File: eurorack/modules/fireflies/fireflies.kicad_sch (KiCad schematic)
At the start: 45 parts, among them J2 AudioJack2_SwitchT, J3 AudioJack2_SwitchT, J4 AudioJack2_SwitchT, J5 AudioJack2_SwitchT, SW1 SW_Push_LED, SW2 SW_Push_LED, U1 MIC5219-5.0YM5, U2 Chordata, U3 MCP4822, U4 TLC5971PWP

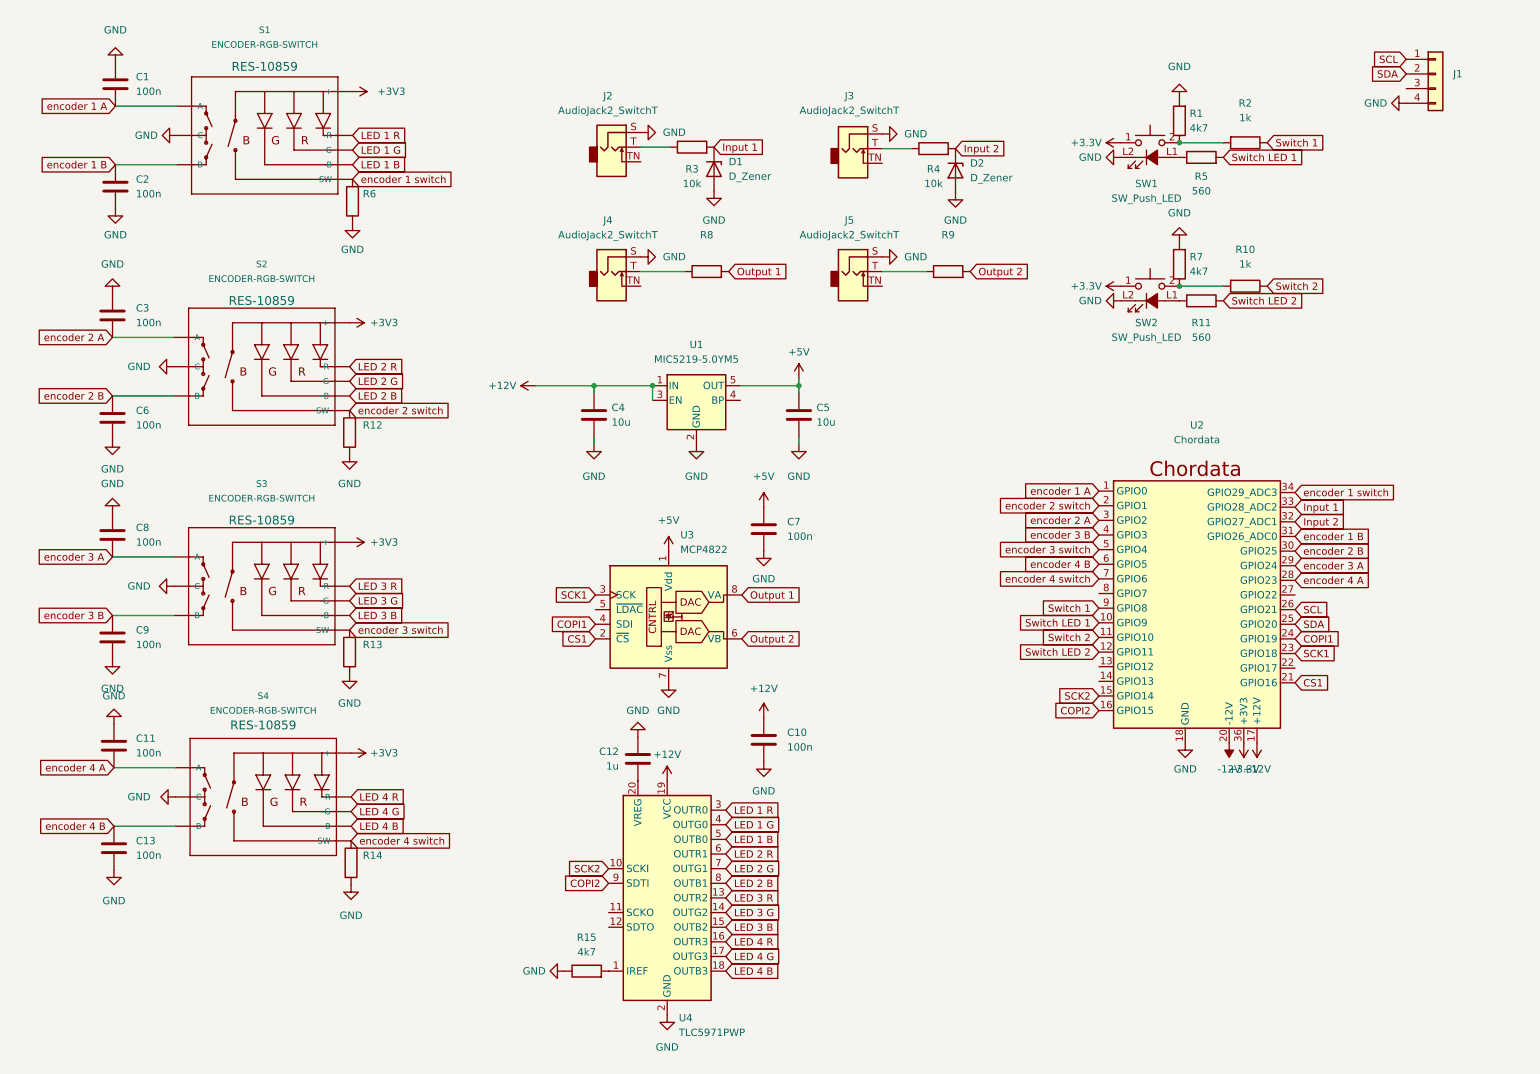
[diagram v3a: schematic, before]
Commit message: wip fireflies redesign
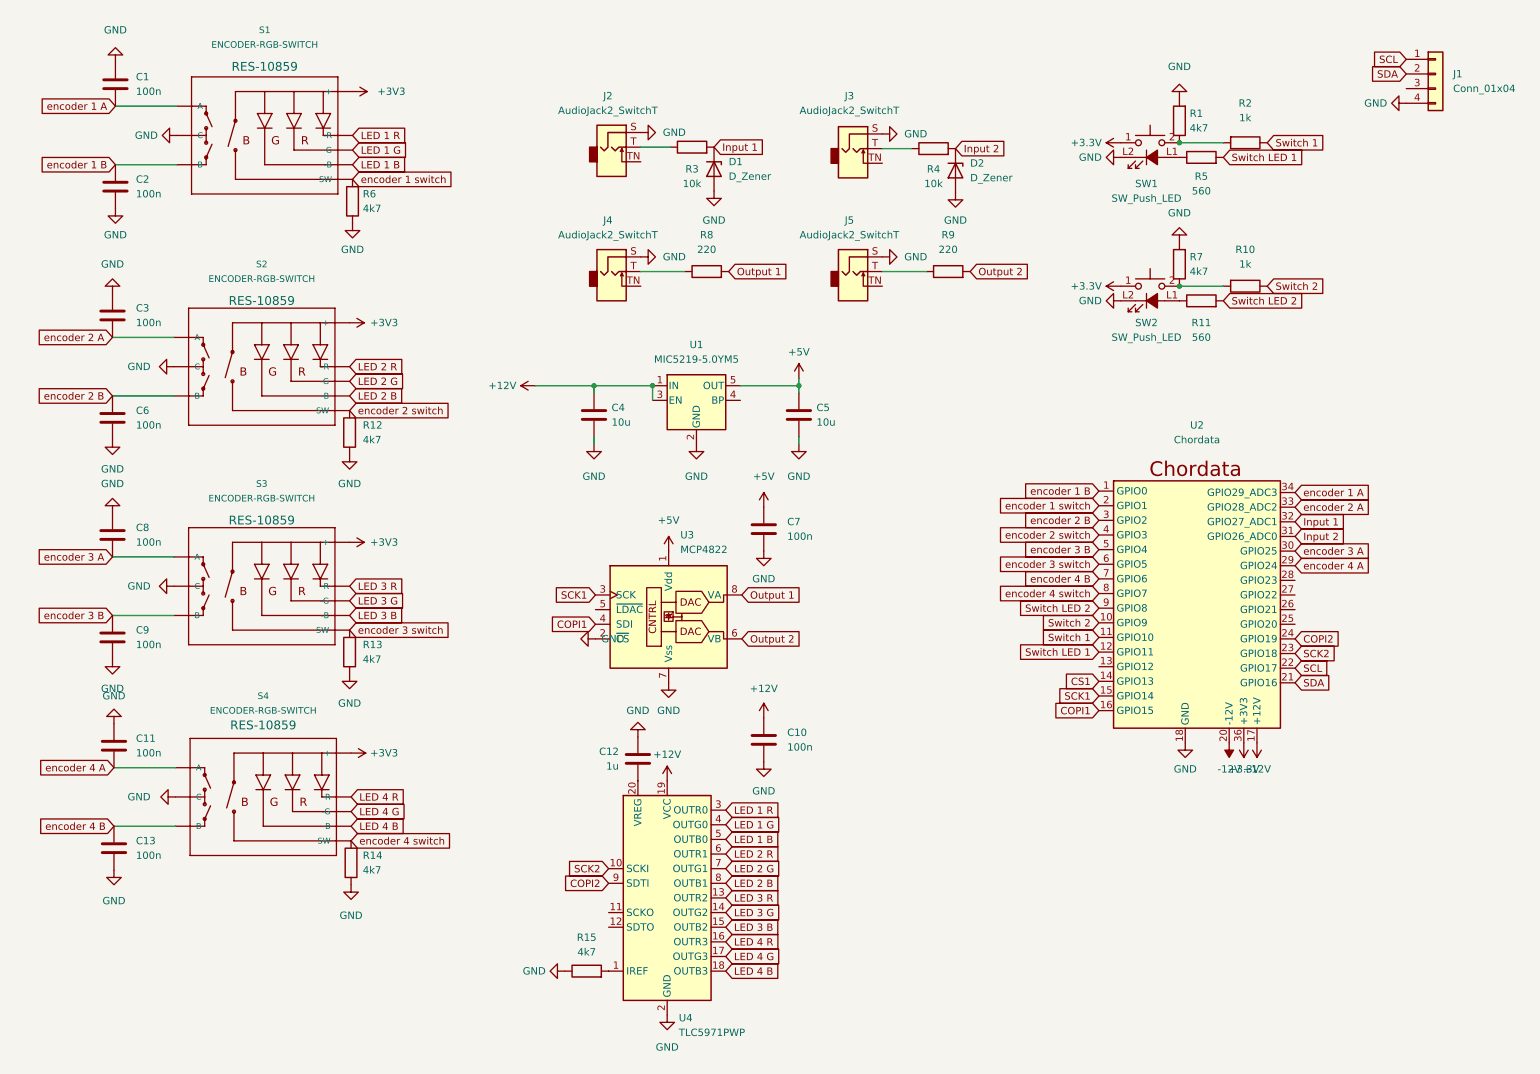
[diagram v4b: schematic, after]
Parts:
- J1: value (none) -> Conn_01x04; footprint (none) -> Pale Slim Ghost:Stemma QT Qwiic JST_SH_SM04B
- R12, R13, R14, R6: value (none) -> 4k7
- R8, R9: value (none) -> 220
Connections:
- net COPI1: now also U2.16 (GPIO15); no longer U2.24 (GPIO19)
- net COPI2: now also U2.24 (GPIO19); no longer U2.16 (GPIO15)
- net CS1: now also U2.14 (GPIO13); no longer U2.21 (GPIO16), U3.2 (~{CS})
- net GND: now also U3.2 (~{CS})
- net Input 1: now also U2.32 (GPIO27_ADC1); no longer U2.33 (GPIO28_ADC2)
- net Input 2: now also U2.31 (GPIO26_ADC0); no longer U2.32 (GPIO27_ADC1)
- net SCK1: now also U2.15 (GPIO14); no longer U2.23 (GPIO18)
- net SCK2: now also U2.23 (GPIO18); no longer U2.15 (GPIO14)
- net SCL: now also U2.22 (GPIO17); no longer U2.26 (GPIO21)
- net SDA: now also U2.21 (GPIO16); no longer U2.25 (GPIO20)
- net Switch 1: now also U2.11 (GPIO10); no longer U2.9 (GPIO8)
- net Switch 2: now also U2.10 (GPIO9); no longer U2.11 (GPIO10)
- net Switch LED 1: now also U2.12 (GPIO11); no longer U2.10 (GPIO9)
- net Switch LED 2: now also U2.9 (GPIO8); no longer U2.12 (GPIO11)
- net encoder 1 A: now also U2.34 (GPIO29_ADC3); no longer U2.1 (GPIO0)
- net encoder 1 B: now also U2.1 (GPIO0); no longer U2.31 (GPIO26_ADC0)
- net encoder 1 switch: now also U2.2 (GPIO1); no longer U2.34 (GPIO29_ADC3)
- net encoder 2 A: now also U2.33 (GPIO28_ADC2); no longer U2.3 (GPIO2)
- net encoder 2 B: now also U2.3 (GPIO2); no longer U2.30 (GPIO25)
- net encoder 2 switch: now also U2.4 (GPIO3); no longer U2.2 (GPIO1)
- net encoder 3 A: now also U2.30 (GPIO25); no longer U2.29 (GPIO24)
- net encoder 3 B: now also U2.5 (GPIO4); no longer U2.4 (GPIO3)
- net encoder 3 switch: now also U2.6 (GPIO5); no longer U2.5 (GPIO4)
- net encoder 4 A: now also U2.29 (GPIO24); no longer U2.28 (GPIO23)
- net encoder 4 B: now also U2.7 (GPIO6); no longer U2.6 (GPIO5)
- net encoder 4 switch: now also U2.8 (GPIO7); no longer U2.7 (GPIO6)

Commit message: i honestly have no idea
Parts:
- removed U1: MIC5219-5.0YM5, Package_TO_SOT_SMD:SOT-23-5, symbol Regulator_Linear:MIC5219-5.0YM5
- added R16, R17, R18, R19: 10k, Resistor_SMD:R_0805_2012Metric_Pad1.20x1.40mm_HandSolder, symbol Device:R
- added U1: TL072, symbol Amplifier_Operational:TL072
- C4, C5: value 10u -> 100n
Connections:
- net +12V: now also C4.2, U1.8 (V+); no longer C4.1
- net +3V3: now also C7.2, U3.1 (Vdd)
- net -12V: now also C5.1, U1.4 (V-)
- net GND: now also C4.1, R16.1, R18.1; no longer C4.2
- net Output 1: now also R17.2, U1.1; no longer U3.8 (VA)
- net Output 2: now also R19.2, U1.7; no longer U3.6 (VB)
- removed net +5V: C5.1, C7.2, U3.1 (Vdd)
- new net: R18.2, R19.1, U1.6 (-)
- new net: R16.2, R17.1, U1.2 (-)
- new net Output 1 raw: U1.3 (+), U3.8 (VA)
- new net Output 2 raw: U1.5 (+), U3.6 (VB)
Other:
- note added: "it's fucking RAWWWWWWW"
- moved on the sheet: C7, D1, D2, J2, J3, J4, J5, R3, R4, R8, R9, U3
